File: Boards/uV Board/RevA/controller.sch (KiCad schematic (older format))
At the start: 2 parts

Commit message: Added a lot to the microVolt board.
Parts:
- added C? (x2): 18pF, symbol Device:C
- added J?: Extra Pins, symbol Connector_Generic:Conn_02x03_Counter_Clockwise
- added R?: 10k, symbol Device:R
- added U?: MCP2515-xSO, Package_SO:SOIC-18W_7.5x11.6mm_P1.27mm, symbol Interface_CAN_LIN:MCP2515-xSO
- added U?: TJA1051T, Package_SO:SOIC-8_3.9x4.9mm_P1.27mm, symbol Interface_CAN_LIN:TJA1051T
- added Y?: 8Mhz, symbol Device:Crystal
- J? (x2): value Conn_01x15_Female -> Arduino Nano
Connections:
- net 5V: now also J?.1 (Pin_1), R?.1, U?.18 (VDD), U?.3 (VCC)
- net GND: now also C?.2, C?.2, J?.6 (Pin_6), U?.2 (GND), U?.8 (S), U?.9 (VSS)
- net SPI_SS: now reaches J?.13 (Pin_13)
- net SPI_SS: now also U?.16 (~CS)
- net SPI_MOSI: now reaches J?.14 (Pin_14)
- net SPI_MOSI: now also U?.14 (SI)
- net SPI_MISO: now reaches J?.15 (Pin_15)
- net SPI_MISO: now also U?.15 (SO)
- net INTERUPT: now reaches J?.5 (Pin_5)
- net INTERUPT: now also U?.12 (~INT)
- net Strain_3: now reaches J?.10 (Pin_10)
- net Strain_2: now reaches J?.11 (Pin_11)
- net Strain_1: now reaches J?.12 (Pin_12)
- net SPI_SCK: now reaches J?.15 (Pin_15)
- net SPI_SCK: now also U?.13 (SCK)
- net Strain_4: now reaches J?.9 (Pin_9)
- new net: U?.1 (TXCAN), U?.1 (TXD)
- new net: R?.2, U?.17 (~RESET)
- new net: U?.2 (RXCAN), U?.4 (RXD)
- new net: C?.1, U?.7 (OSC2), Y?.2
- new net: C?.1, U?.8 (OSC1), Y?.1
- new net Analog1: J?.2 (Pin_2)
- new net Analog2: J?.3 (Pin_3)
- new net CAN_H: U?.7 (CANH)
- new net CAN_L: U?.6 (CANL)
- new net DIO1: J?.5 (Pin_5)
- new net DIO2: J?.4 (Pin_4)
- no-connect marks 0 -> 23
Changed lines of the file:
@@
 $Descr A4 11693 8268
 encoding utf-8
-Sheet 2 4
+Sheet 2 6
 Title ""
 Date ""
@@
 P 1600 1550
 F 0 "J?" H 1628 1576 50  0000 L CNN
-F 1 "Conn_01x15_Female" H 1628 1485 50  0000 L CNN
+F 1 "Arduino Nano" H 1628 1485 50  0000 L CNN
 F 2 "" H 1600 1550 50  0001 C CNN
 F 3 "~" H 1600 1550 50  0001 C CNN
@@
 	1    0    0    -1
 $EndComp
+Text HLabel 3000 950  0    50   Input ~ 0
+GND
+Text HLabel 3000 850  0    50   Input ~ 0
+5V
+Text HLabel 1400 1150 0    50   Input ~ 0
+GND
+Text HLabel 1400 1050 0    50   Input ~ 0
+Reset
+NoConn ~ 1400 850
+NoConn ~ 1400 950
+NoConn ~ 1400 1350
+NoConn ~ 1400 1450
+NoConn ~ 1400 1550
+NoConn ~ 1400 1650
+NoConn ~ 1400 1750
+NoConn ~ 1400 1850
+NoConn ~ 1400 1950
+NoConn ~ 3000 2150
+NoConn ~ 3000 2050
+NoConn ~ 3000 1550
+NoConn ~ 3000 1450
+NoConn ~ 3000 1350
+NoConn ~ 3000 1250
+NoConn ~ 3000 1150
+NoConn ~ 3000 1050
 $Comp
 L Connector:Conn_01x15_Female J?
@@
 P 3200 1550
 F 0 "J?" H 3228 1576 50  0000 L CNN
-F 1 "Conn_01x15_Female" H 3228 1485 50  0000 L CNN
+F 1 "Arduino Nano" H 3228 1485 50  0000 L CNN
 F 2 "" H 3200 1550 50  0001 C CNN
 F 3 "~" H 3200 1550 50  0001 C CNN
@@
 	1    0    0    -1
 $EndComp
-Text HLabel 3000 950  0    50   Input ~ 0
-GND
-Text HLabel 3000 850  0    50   Input ~ 0
-5V
-Text HLabel 1400 1150 0    50   Input ~ 0
-GND
-Text HLabel 1400 1050 0    50   Input ~ 0
-Reset
+$Comp
+L Interface_CAN_LIN:MCP2515-xSO U?
+U 1 1 61540764
+P 3300 3650
+F 0 "U?" H 3300 4631 50  0000 C CNN
+F 1 "MCP2515-xSO" H 3300 4540 50  0000 C CNN
+F 2 "Package_SO:SOIC-18W_7.5x11.6mm_P1.27mm" H 3300 2750 50  0001 C CIN
+F 3 "http://ww1.microchip.com/downloads/en/DeviceDoc/21801e.pdf" H 3400 2850 50  0001 C CNN
+	1    3300 3650
+	1    0    0    -1
+$EndComp
+$Comp
+L Interface_CAN_LIN:TJA1051T U?
+U 1 1 61542279
+P 5200 3550
+F 0 "U?" H 5200 4131 50  0000 C CNN
+F 1 "TJA1051T" H 5200 4040 50  0000 C CNN
+F 2 "Package_SO:SOIC-8_3.9x4.9mm_P1.27mm" H 5200 3050 50  0001 C CIN
+F 3 "http://www.nxp.com/documents/data_sheet/TJA1051.pdf" H 5200 3550 50  0001 C CNN
+	1    5200 3550
+	1    0    0    -1
+$EndComp
+Wire Wire Line
+	4700 3450 4000 3450
+Wire Wire Line
+	4000 3450 4000 3050
+Wire Wire Line
+	4000 3050 3900 3050
+Wire Wire Line
+	3900 3150 4700 3150
+Wire Wire Line
+	4700 3150 4700 3350
+$Comp
+L Device:Crystal Y?
+U 1 1 6154565E
+P 2150 4500
+F 0 "Y?" H 2150 4768 50  0000 C CNN
+F 1 "8Mhz" H 2150 4677 50  0000 C CNN
+F 2 "" H 2150 4500 50  0001 C CNN
+F 3 "~" H 2150 4500 50  0001 C CNN
+	1    2150 4500
+	1    0    0    -1
+$EndComp
+Wire Wire Line
+	2700 3850 2300 3850
+Wire Wire Line
+	2300 3850 2300 4500
+Wire Wire Line
+	2700 3950 2000 3950
+Wire Wire Line
+	2000 3950 2000 4500
+$Comp
+L Device:C C?
+U 1 1 61547480
+P 2000 4850
+F 0 "C?" H 2115 4896 50  0000 L CNN
+F 1 "18pF" H 2115 4805 50  0000 L CNN
+F 2 "" H 2038 4700 50  0001 C CNN
+F 3 "~" H 2000 4850 50  0001 C CNN
+	1    2000 4850
+	1    0    0    -1
+$EndComp
+Wire Wire Line
+	2300 4500 2300 4700
+Connection ~ 2300 4500
+Wire Wire Line
+	2000 4500 2000 4700
+Connection ~ 2000 4500
+Text HLabel 3300 4450 3    50   Input ~ 0
+GND
+Text HLabel 2000 5000 3    50   Input ~ 0
+GND
+Text HLabel 5200 3950 3    50   Input ~ 0
+GND
+NoConn ~ 2700 4050
+NoConn ~ 3900 3750
+NoConn ~ 3900 3850
+NoConn ~ 3900 3950
+NoConn ~ 3900 4050
+NoConn ~ 3900 4150
+Text HLabel 3300 2850 0    50   Input ~ 0
+5V
+$Comp
+L Device:R R?
+U 1 1 6154D1B1
+P 4050 4250
+F 0 "R?" V 3843 4250 50  0000 C CNN
+F 1 "10k" V 3934 4250 50  0000 C CNN
+F 2 "" V 3980 4250 50  0001 C CNN
+F 3 "~" H 4050 4250 50  0001 C CNN
+	1    4050 4250
+	0    1    1    0
+$EndComp
+Wire Wire Line
+	4200 4250 4350 4250
+Wire Wire Line
+	4350 4250 4350 2850
+Wire Wire Line
+	4350 2850 3300 2850
+Text HLabel 5200 3150 0    50   Input ~ 0
+5V
+Text HLabel 4700 3750 0    50   Input ~ 0
+GND
+$Comp
+L Device:C C?
+U 1 1 61552802
+P 2300 4850
+F 0 "C?" H 2415 4896 50  0000 L CNN
+F 1 "18pF" H 2415 4805 50  0000 L CNN
+F 2 "" H 2338 4700 50  0001 C CNN
+F 3 "~" H 2300 4850 50  0001 C CNN
+	1    2300 4850
+	1    0    0    -1
+$EndComp
+Text HLabel 2300 5000 3    50   Input ~ 0
+GND
+Text HLabel 5700 3450 2    50   Input ~ 0
+CAN_H
+Text HLabel 5700 3650 2    50   Input ~ 0
+CAN_L
+$Comp
+L Connector_Generic:Conn_02x03_Counter_Clockwise J?
+U 1 1 61567E78
+P 4800 1100
+F 0 "J?" H 4850 1417 50  0000 C CNN
+F 1 "Extra Pins" H 4850 1326 50  0000 C CNN
+F 2 "" H 4800 1100 50  0001 C CNN
+F 3 "~" H 4800 1100 50  0001 C CNN
+	1    4800 1100
+	1    0    0    -1
+$EndComp
+Text HLabel 4600 1000 0    50   Input ~ 0
+5V
+Text Label 5100 1100 0    50   ~ 0
+DIO1
+Text Label 5100 1200 0    50   ~ 0
+DIO2
+Text Label 4600 1100 2    50   ~ 0
+Analog1
+Text Label 4600 1200 2    50   ~ 0
+Analog2
+Text HLabel 5100 1000 2    50   Input ~ 0
+GND
+Text Label 3900 3650 0    50   ~ 0
+INTERUPT
+Text Label 1400 1250 2    50   ~ 0
+INTERUPT
+Text Label 1400 2050 2    50   ~ 0
+SPI_SS
+Text Label 2700 3250 2    50   ~ 0
+SPI_SS
+Text Label 1400 2150 2    50   ~ 0
+SPI_MOSI
+Text Label 2700 3150 2    50   ~ 0
+SPI_MISO
+Text Label 3000 2250 2    50   ~ 0
+SPI_SCK
+Text Label 2700 3050 2    50   ~ 0
+SPI_MOSI
+Text Label 1400 2250 2    50   ~ 0
+SPI_MISO
+Text Label 2700 3350 2    50   ~ 0
+SPI_SCK
+Text HLabel 3000 1650 0    50   Input ~ 0
+Strain_4
+Text HLabel 3000 1750 0    50   Input ~ 0
+Strain_3
+Text HLabel 3000 1850 0    50   Input ~ 0
+Strain_2
+Text HLabel 3000 1950 0    50   Input ~ 0
+Strain_1
 $EndSCHEMATC

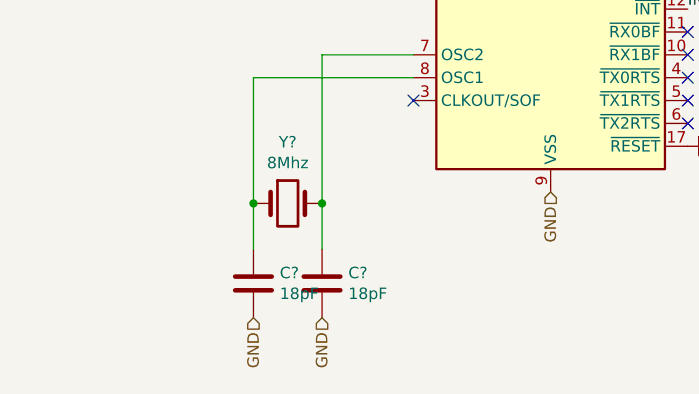
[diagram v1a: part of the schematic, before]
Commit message: Created Rev_B of the MicroVolt Board. Edited RevA of ADC Board.
Deleted CAN infrastructure in Rev_B, and added I2C "infrastructure." Better labeled arduino nano pins within controller sheet. Imported pins from controller sheet out to board. Added controller, pull up and pulldown resistor sheets, and a button inputs sheet.
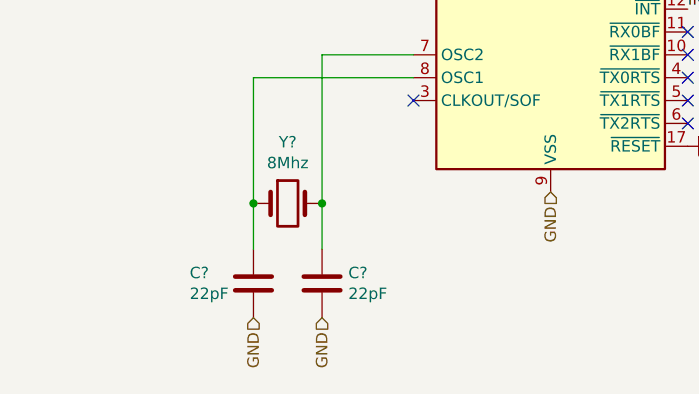
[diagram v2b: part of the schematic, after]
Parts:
- C? (x2): value 18pF -> 22pF
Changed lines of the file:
@@
 U 1 1 61547480
 P 2000 4850
-F 0 "C?" H 2115 4896 50  0000 L CNN
-F 1 "18pF" H 2115 4805 50  0000 L CNN
+F 0 "C?" H 1721 4896 50  0000 L CNN
+F 1 "22pF" H 1721 4805 50  0000 L CNN
 F 2 "" H 2038 4700 50  0001 C CNN
 F 3 "~" H 2000 4850 50  0001 C CNN
@@
 P 2300 4850
 F 0 "C?" H 2415 4896 50  0000 L CNN
-F 1 "18pF" H 2415 4805 50  0000 L CNN
+F 1 "22pF" H 2415 4805 50  0000 L CNN
 F 2 "" H 2338 4700 50  0001 C CNN
 F 3 "~" H 2300 4850 50  0001 C CNN
